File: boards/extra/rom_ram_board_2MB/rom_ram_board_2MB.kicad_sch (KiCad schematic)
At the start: 32 parts, among them J1 Exp. Conn. A, J2 Power, U1 74LS04, U10 AS6C4008-55PCN, U2 74LS30, U3 74LS32, U5 74LS670, U5 SST39SF040, U6 74LS244, U7 AS6C4008-55PCN, U8 74LS139, U9 AS6C4008-55PCN

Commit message: * Working on new powerdistribution method.
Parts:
- removed J2: Power, Connector_IDC:IDC-Header_2x10_P2.54mm_Horizontal, symbol Connector_Generic:Conn_02x10_Top_Bottom
- added J3: Power, footprints:TE_171826-4, symbol Connector_Generic:Conn_01x04
- R3: value 470 -> 1k
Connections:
- net +5V3 is gone; now on net +5V: C1.1, C1.1, C2.1, C2.1, C2.1, C2.1, C2.1, C2.1, C2.1, C2.1, C2.1, CP1.1, CP2.1, R3.1, U1.14 (VCC), U10.32 (VCC), U2.14 (VCC), U3.14 (VCC), U5.16 (VCC), U5.16 (VCC), U5.31 (PGM), U5.32 (VCC), U6.20 (VCC), U7.32 (VCC), U8.16 (VCC), U9.32 (VCC)
- net +5V: now also J3.4 (Pin_4)
- net GND: now also J3.2 (Pin_2), J3.3 (Pin_3)
- no-connect marks 39 -> 28

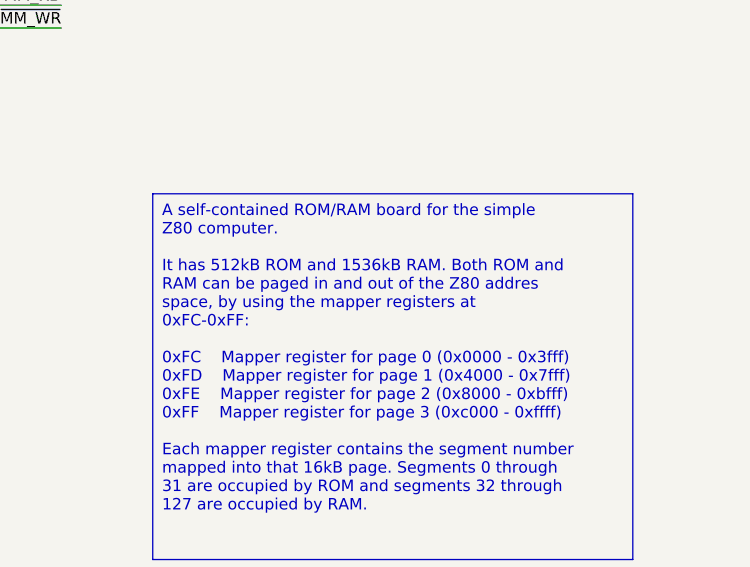
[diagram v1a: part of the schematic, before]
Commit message: Added expansion connector C and designed some new boards around it.
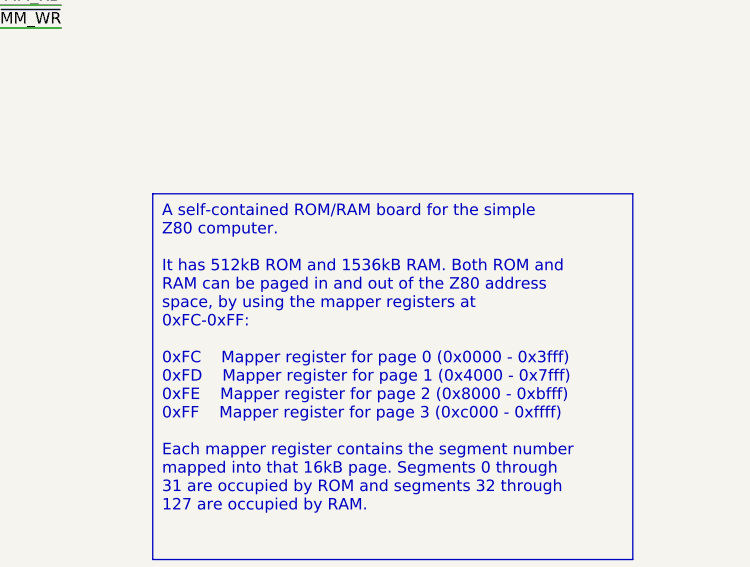
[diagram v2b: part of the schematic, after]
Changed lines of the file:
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@@
     (stroke (width 0) (type default))
   )
-  (text_box "A self-contained ROM/RAM board for the simple Z80 computer. \n\nIt has 512kB ROM and 1536kB RAM. Both ROM and RAM can be paged in and out of the Z80 addres space, by using the mapper registers at 0xFC-0xFF:\n\n0xFC	Mapper register for page 0 (0x0000 - 0x3fff)\n0xFD	Mapper register for page 1 (0x4000 - 0x7fff)\n0xFE	Mapper register for page 2 (0x8000 - 0xbfff)\n0xFF	Mapper register for page 3 (0xc000 - 0xffff)\n\nEach mapper register contains the segment number mapped into that 16kB page. Segments 0 through 31 are occupied by ROM and segments 32 through 127 are occupied by RAM."
+  (text_box "A self-contained ROM/RAM board for the simple Z80 computer. \n\nIt has 512kB ROM and 1536kB RAM. Both ROM and RAM can be paged in and out of the Z80 address space, by using the mapper registers at 0xFC-0xFF:\n\n0xFC	Mapper register for page 0 (0x0000 - 0x3fff)\n0xFD	Mapper register for page 1 (0x4000 - 0x7fff)\n0xFE	Mapper register for page 2 (0x8000 - 0xbfff)\n0xFF	Mapper register for page 3 (0xc000 - 0xffff)\n\nEach mapper register contains the segment number mapped into that 16kB page. Segments 0 through 31 are occupied by ROM and segments 32 through 127 are occupied by RAM."
     (at 352.425 210.82 0) (size 53.34 40.64)
     (stroke (width 0) (type default))
